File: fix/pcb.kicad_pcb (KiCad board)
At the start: 2 copper layers, 109 x 54 mm, 64 parts, among them J1 MALE, J10 TC2030_NL, J101 MALE, J102 FEMALE, J103 MALE, J104 FEMALE, J105 MALE, J106 FEMALE, J107 MALE, J108 FEMALE, J11 STANDOFF, J111 STANDOFF, J112 STANDOFF, J113 STANDOFF, J114 STANDOFF, J12 STANDOFF, J13 STANDOFF, J14 STANDOFF, J2 FEMALE, J3 MALE, J4 FEMALE, J5 MALE, J6 FEMALE, J7 MALE, J8 FEMALE, J9 DTR, Q1 2N3904, SW1 ACTION, SW2 ACTION, SW3 ACTION, SW4 ACTION, U3 ATmega328P-MU, Y1 YSX321SL

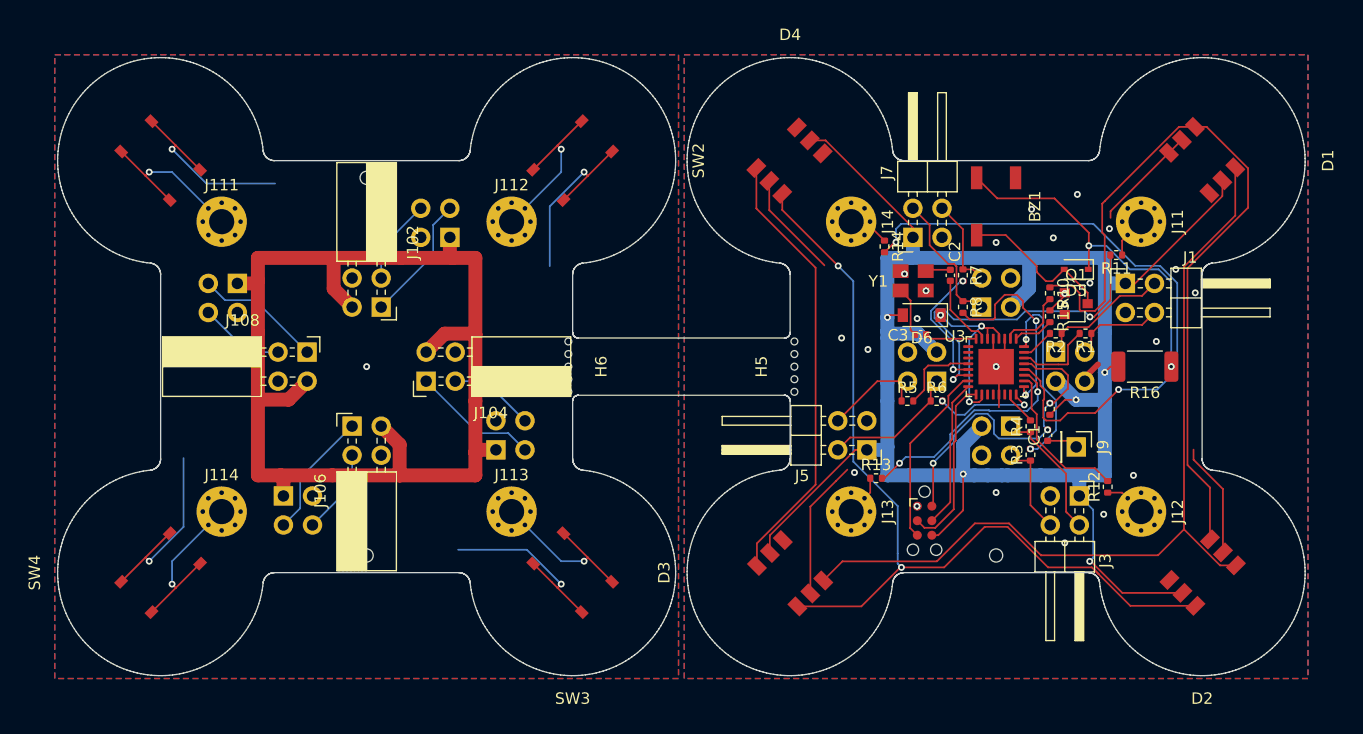
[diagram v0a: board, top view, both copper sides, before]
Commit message: Fix fix: Wrong wiring for new males
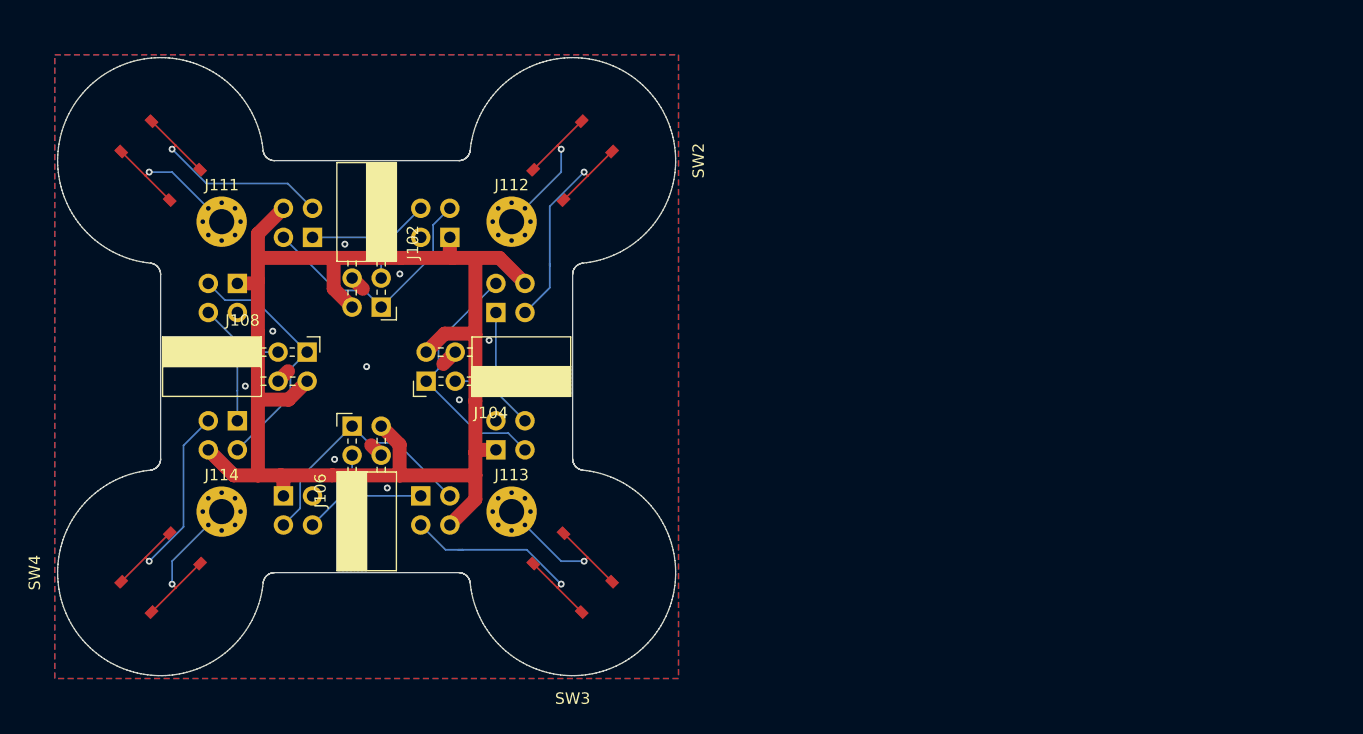
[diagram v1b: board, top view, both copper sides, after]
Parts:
- removed BZ1: Buzzer, node:MLT-5020
- removed C1: 100n, Capacitor_SMD:C_0402_1005Metric
- removed C2, C3: 12p, Capacitor_SMD:C_0402_1005Metric
- removed D1, D2, D3, D4: WS2813, node:bottom-leaf
- removed D5: 1N4148, Diode_SMD:D_SOD-323
- removed D6: B5819W, Diode_SMD:D_SOD-123
- removed H1, H2, H3: MountingHole, node:JLCPCB-tooling-hole
- removed H5, H6: Mouse_bite, node:single_sided_tab_5mm
- removed J1, J3, J5, J7: MALE, Connector_PinHeader_2.54mm:PinHeader_2x02_P2.54mm_Horizontal
- removed J10: TC2030_NL, Connector:Tag-Connect_TC2030-IDC-NL_2x03_P1.27mm_Vertical
- removed J11, J12, J13, J14: STANDOFF, MountingHole:MountingHole_2.2mm_M2_Pad_Via
- removed J2, J4, J6, J8: FEMALE, Connector_PinSocket_2.54mm:PinSocket_2x02_P2.54mm_Horizontal
- removed J9: DTR, Connector_PinHeader_2.54mm:PinHeader_1x01_P2.54mm_Vertical
- removed Q1: 2N3904, Package_TO_SOT_SMD:SOT-23
- removed R1, R10, R11, R12, R13, R14, R15, R2, R3, R4, R5, R6, R7, R8: 470, Resistor_SMD:R_0402_1005Metric
- removed R16: 22 0.5W, Resistor_SMD:R_2010_5025Metric
- removed R9: 10K, Resistor_SMD:R_0402_1005Metric
- removed U3: ATmega328P-MU, Package_DFN_QFN:QFN-32-1EP_5x5mm_P0.5mm_EP3.1x3.1mm
- removed Y1: YSX321SL, node:YSX321SL
- added J1010: MALE, Connector_PinHeader_2.54mm:PinHeader_2x02_P2.54mm_Horizontal, B.Cu at (116.3, 93.7)
- added J1030: MALE, Connector_PinHeader_2.54mm:PinHeader_2x02_P2.54mm_Horizontal, B.Cu at (132.3, 100.3)
- added J1050: MALE, Connector_PinHeader_2.54mm:PinHeader_2x02_P2.54mm_Horizontal, B.Cu at (125.7, 116.3)
- added J1070: MALE, Connector_PinHeader_2.54mm:PinHeader_2x02_P2.54mm_Horizontal, B.Cu at (109.7, 109.7)
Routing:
- net +5VB: track 172.7 -> 0.00 mm, vias 5 -> 0
- net Net-(D2-Pad3): track 78.0 -> 0.00 mm, vias 2 -> 0
- net Net-(D1-Pad3): track 75.0 -> 0.00 mm
- net /Lower Board/DIN: track 68.0 -> 0.00 mm
- net Net-(R14-Pad2): track 55.9 -> 0.00 mm, vias 2 -> 0
- net GNDB: track 52.4 -> 0.00 mm, vias 22 -> 0
- net Net-(D3-Pad3): track 39.0 -> 0.00 mm
- net Net-(BZ1-Pad1): track 30.9 -> 0.00 mm, vias 2 -> 0
- net Net-(R11-Pad2): track 29.4 -> 0.00 mm, vias 2 -> 0
- net /Lower Board/~RST: track 28.2 -> 0.00 mm, vias 3 -> 0
- net GND: track 66.0 -> 89.4 mm, vias 5 -> 13
- net +5V: track 104.2 -> 125.2 mm
- net Net-(R13-Pad2): track 19.8 -> 0.00 mm, vias 2 -> 0
- net Net-(R3-Pad2): track 17.8 -> 0.00 mm, vias 2 -> 0
- net Net-(R8-Pad2): track 17.2 -> 0.00 mm, vias 2 -> 0
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- removed copper zone on B.Cu, net GNDB
- removed copper zone on F.Cu, net GNDB
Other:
- board size 109 x 54 mm -> 54 x 54 mm

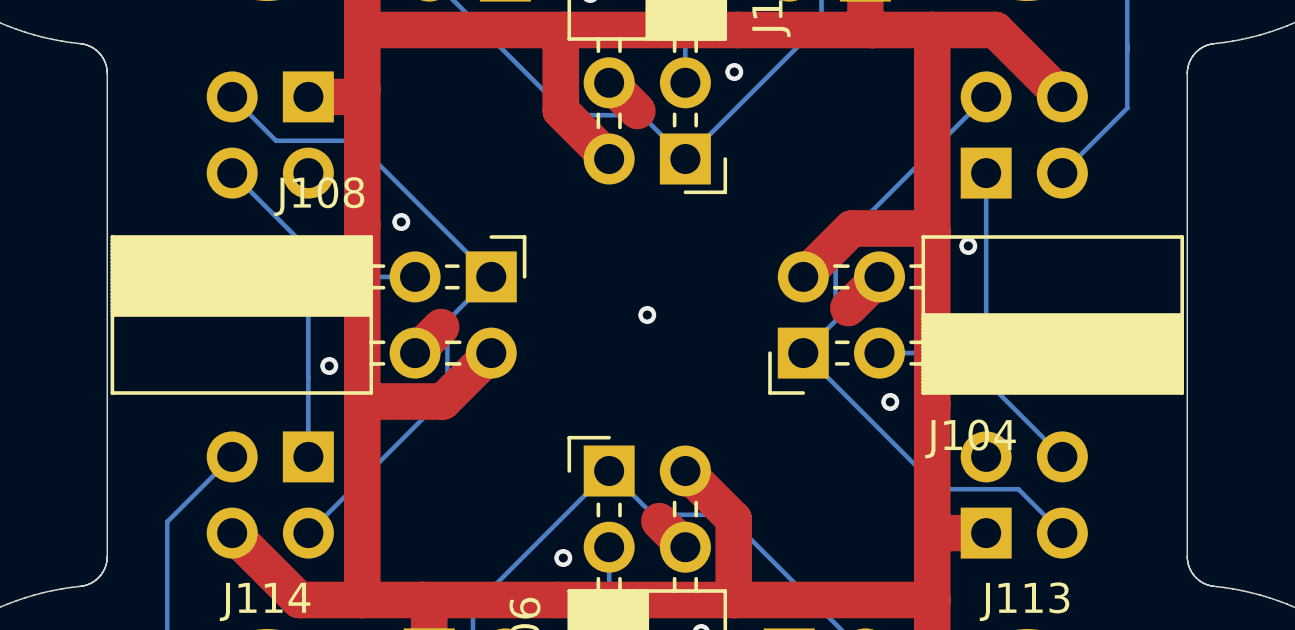
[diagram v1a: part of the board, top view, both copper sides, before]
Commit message: Add mounting holes for PCBA
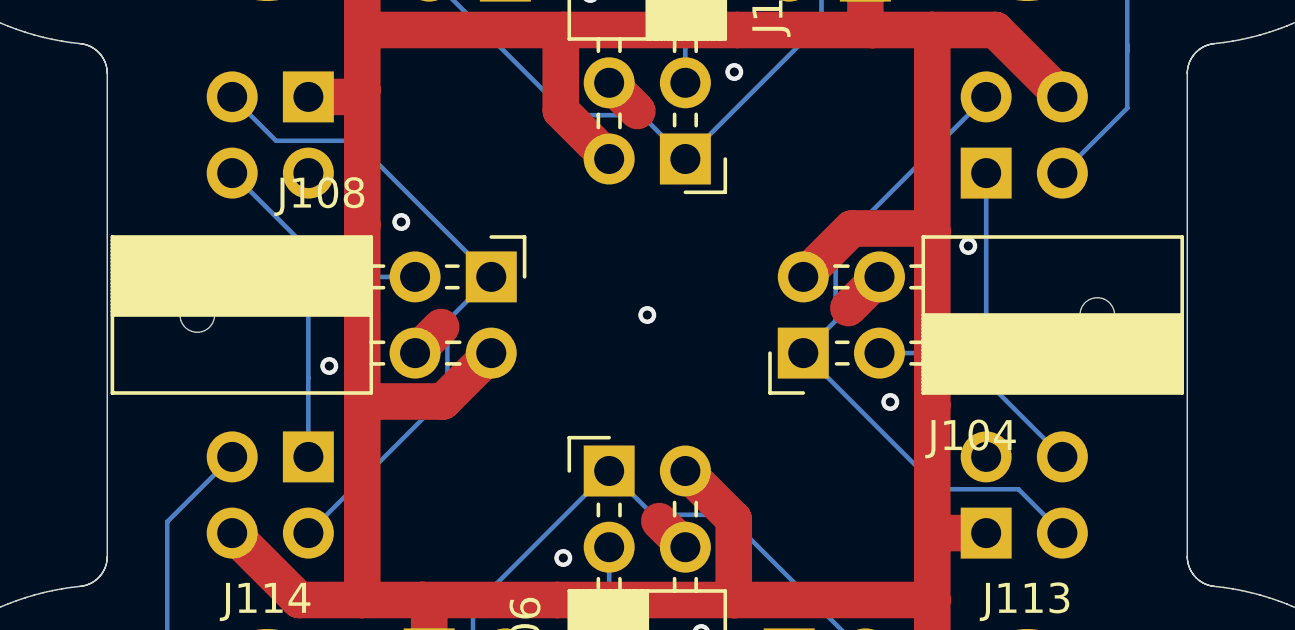
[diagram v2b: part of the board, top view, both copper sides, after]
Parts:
- added H1: MountingHole, node:JLCPCB-tooling-hole, F.Cu at (136.0, 105.0)
- added H2: MountingHole, node:JLCPCB-tooling-hole, F.Cu at (106.0, 105.0)
